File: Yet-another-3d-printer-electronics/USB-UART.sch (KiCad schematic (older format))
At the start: 13 parts

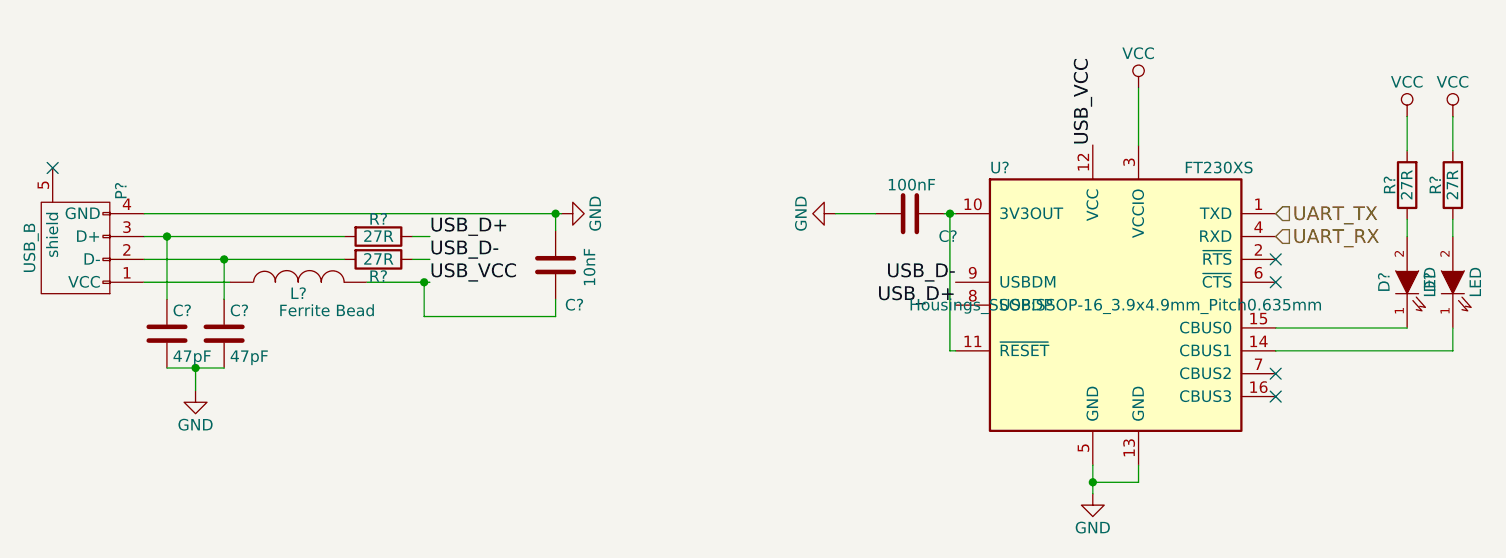
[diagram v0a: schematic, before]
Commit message: Add power section and remove fan heater
Add aoz1284pi buck conventer.

Signed-off-by: Mateusz Krawczuk <mat.krawczuk@gmail.com>
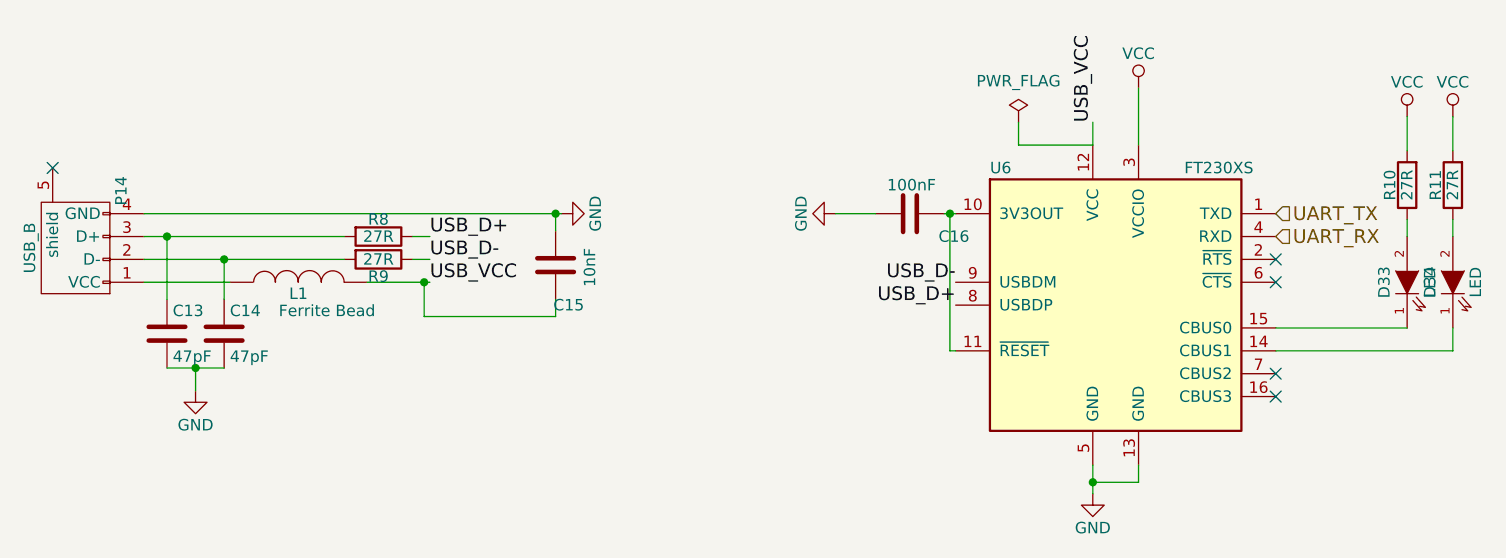
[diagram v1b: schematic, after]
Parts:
- gave numbers to parts that had none: 13
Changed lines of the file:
@@
 LIBS:valves
 LIBS:ftdi
+LIBS:aoz1284pi
 LIBS:Yet-another-3d-printer-electronics-cache
 EELAYER 25 0
@@
 $Descr A4 11693 8268
 encoding utf-8
-Sheet 3 4
+Sheet 3 5
 Title ""
 Date ""
@@
 NoConn ~ 7775 3175
 $Comp
-L FT230XS U?
+L FT230XS U6
 U 1 1 58B1D6DF
 P 7075 3375
-F 0 "U?" H 6525 3975 50  0000 L CNN
+F 0 "U6" H 6525 3975 50  0000 L CNN
 F 1 "FT230XS" H 7375 3975 50  0000 L CNN
-F 2 "Housings_SSOP:SSOP-16_3.9x4.9mm_Pitch0.635mm" H 7075 3375 50  0000 C CNN
+F 2 "Housings_SSOP:SSOP-16_3.9x4.9mm_Pitch0.635mm" H 7075 3375 50  0001 C CNN
 F 3 "" H 7075 3375 50  0000 C CNN
 	1    7075 3375
@@
 NoConn ~ 7775 3775
 $Comp
-L VCC #PWR?
+L VCC #PWR061
 U 1 1 58B1D6E9
 P 7175 2425
-F 0 "#PWR?" H 7175 2275 50  0001 C CNN
+F 0 "#PWR061" H 7175 2275 50  0001 C CNN
 F 1 "VCC" H 7175 2575 50  0000 C CNN
 F 2 "" H 7175 2425 50  0000 C CNN
@@
 $EndComp
 $Comp
-L GND #PWR?
+L GND #PWR062
 U 1 1 58B1D6EF
 P 6975 4200
-F 0 "#PWR?" H 6975 3950 50  0001 C CNN
+F 0 "#PWR062" H 6975 3950 50  0001 C CNN
 F 1 "GND" H 6975 4050 50  0000 C CNN
 F 2 "" H 6975 4200 50  0000 C CNN
@@
 $EndComp
 $Comp
-L USB_B-RESCUE-Yet-another-3d-printer-electronics P?
+L USB_B-RESCUE-Yet-another-3d-printer-electronics P14
 U 1 1 58B1D6F5
 P 2525 3075
-F 0 "P?" H 2725 2875 50  0000 C CNN
+F 0 "P14" H 2725 2875 50  0000 C CNN
 F 1 "USB_B" H 2475 3275 50  0000 C CNN
 F 2 "Connect:USB_B" V 2475 2975 50  0001 C CNN
@@
 $EndComp
 $Comp
-L R R?
+L R R8
 U 1 1 58B1D6FC
 P 3850 3075
-F 0 "R?" V 3775 3075 50  0000 C CNN
+F 0 "R8" V 3775 3075 50  0000 C CNN
 F 1 "27R" V 3850 3075 50  0000 C CNN
 F 2 "Resistors_SMD:R_0805_HandSoldering" V 3780 3075 50  0001 C CNN
@@
 $EndComp
 $Comp
-L R R?
+L R R9
 U 1 1 58B1D703
 P 3850 3175
-F 0 "R?" V 3925 3175 50  0000 C CNN
+F 0 "R9" V 3925 3175 50  0000 C CNN
 F 1 "27R" V 3850 3175 50  0000 C CNN
 F 2 "Resistors_SMD:R_0805_HandSoldering" V 3780 3175 50  0001 C CNN
@@
 USB_D-
 $Comp
-L C C?
+L C C16
 U 1 1 58B1D70C
 P 6175 2975
-F 0 "C?" V 6275 3100 50  0000 L CNN
+F 0 "C16" V 6275 3100 50  0000 L CNN
 F 1 "100nF" V 6050 2875 50  0000 L CNN
 F 2 "Capacitors_SMD:C_0805_HandSoldering" H 6213 2825 50  0001 C CNN
@@
 $EndComp
 $Comp
-L GND #PWR?
+L GND #PWR063
 U 1 1 58B1D713
 P 5850 2975
-F 0 "#PWR?" H 5850 2725 50  0001 C CNN
+F 0 "#PWR063" H 5850 2725 50  0001 C CNN
 F 1 "GND" H 5850 2825 50  0000 C CNN
 F 2 "" H 5850 2975 50  0000 C CNN
@@
 	0    1    1    0
 $EndComp
-Text Label 6975 2675 1    60   ~ 0
+Text Label 6975 2575 1    60   ~ 0
 USB_VCC
 $Comp
-L C C?
-U 1 1 58B1D71A
-P 2925 3500
-F 0 "C?" H 2950 3600 50  0000 L CNN
-F 1 "47pF" H 2950 3400 50  0000 L CNN
-F 2 "Capacitors_SMD:C_0805_HandSoldering" H 2963 3350 50  0001 C CNN
-F 3 "" H 2925 3500 50  0000 C CNN
-	1    2925 3500
-	1    0    0    -1
-$EndComp
-$Comp
-L C C?
+L C C14
 U 1 1 58B1D721
 P 3175 3500
-F 0 "C?" H 3200 3600 50  0000 L CNN
+F 0 "C14" H 3200 3600 50  0000 L CNN
 F 1 "47pF" H 3200 3400 50  0000 L CNN
 F 2 "Capacitors_SMD:C_0805_HandSoldering" H 3213 3350 50  0001 C CNN
@@
 NoConn ~ 2425 2775
 $Comp
-L GND #PWR?
+L GND #PWR064
 U 1 1 58B1D729
 P 3050 3750
-F 0 "#PWR?" H 3050 3500 50  0001 C CNN
+F 0 "#PWR064" H 3050 3500 50  0001 C CNN
 F 1 "GND" H 3050 3600 50  0000 C CNN
 F 2 "" H 3050 3750 50  0000 C CNN
@@
 USB_VCC
 $Comp
-L GND #PWR?
+L GND #PWR065
 U 1 1 58B1D732
 P 4650 2975
-F 0 "#PWR?" H 4650 2725 50  0001 C CNN
+F 0 "#PWR065" H 4650 2725 50  0001 C CNN
 F 1 "GND" H 4650 2825 50  0000 C CNN
 F 2 "" H 4650 2975 50  0000 C CNN
@@
 $EndComp
 $Comp
-L C C?
+L C C15
 U 1 1 58B1D738
 P 4625 3200
-F 0 "C?" H 4500 3375 50  0000 L CNN
+F 0 "C15" H 4500 3375 50  0000 L CNN
 F 1 "10nF" V 4475 3125 50  0000 L CNN
 F 2 "Capacitors_SMD:C_0805_HandSoldering" H 4663 3050 50  0001 C CNN
@@
 $EndComp
 $Comp
-L INDUCTOR L?
+L INDUCTOR L1
 U 1 1 58B1D73F
 P 3500 3275
-F 0 "L?" V 3450 3275 50  0000 C CNN
+F 0 "L1" V 3450 3275 50  0000 C CNN
 F 1 "Ferrite Bead" V 3375 3150 50  0000 C CNN
 F 2 "Choke_SMD:Choke_SMD_Wuerth-WE-PDF_Handsoldering" H 3500 3275 50  0001 C CNN
@@
 $EndComp
 $Comp
-L LED-RESCUE-Yet-another-3d-printer-electronics D?
+L LED-RESCUE-Yet-another-3d-printer-electronics D33
 U 1 1 58B1D746
 P 8350 3275
-F 0 "D?" H 8350 3375 50  0000 C CNN
+F 0 "D33" H 8350 3375 50  0000 C CNN
 F 1 "LED" H 8350 3175 50  0000 C CNN
 F 2 "LEDs:LED_0805" H 8350 3275 50  0001 C CNN
@@
 $EndComp
 $Comp
-L LED-RESCUE-Yet-another-3d-printer-electronics D?
+L LED-RESCUE-Yet-another-3d-printer-electronics D34
 U 1 1 58B1D74D
 P 8550 3275
-F 0 "D?" H 8550 3375 50  0000 C CNN
+F 0 "D34" H 8550 3375 50  0000 C CNN
 F 1 "LED" H 8550 3175 50  0000 C CNN
 F 2 "LEDs:LED_0805" H 8550 3275 50  0001 C CNN
@@
 $EndComp
 $Comp
-L R R?
+L R R10
 U 1 1 58B1D754
 P 8350 2850
-F 0 "R?" V 8425 2850 50  0000 C CNN
+F 0 "R10" V 8425 2850 50  0000 C CNN
 F 1 "27R" V 8350 2850 50  0000 C CNN
 F 2 "Resistors_SMD:R_0805_HandSoldering" V 8280 2850 50  0001 C CNN
@@
 $EndComp
 $Comp
-L R R?
+L R R11
 U 1 1 58B1D75B
 P 8550 2850
-F 0 "R?" V 8625 2850 50  0000 C CNN
+F 0 "R11" V 8625 2850 50  0000 C CNN
 F 1 "27R" V 8550 2850 50  0000 C CNN
 F 2 "Resistors_SMD:R_0805_HandSoldering" V 8480 2850 50  0001 C CNN
@@
 $EndComp
 $Comp
-L VCC #PWR?
+L VCC #PWR066
 U 1 1 58B1D762
 P 8350 2550
-F 0 "#PWR?" H 8350 2400 50  0001 C CNN
+F 0 "#PWR066" H 8350 2400 50  0001 C CNN
 F 1 "VCC" H 8350 2700 50  0000 C CNN
 F 2 "" H 8350 2550 50  0000 C CNN
@@
 $EndComp
 $Comp
-L VCC #PWR?
+L VCC #PWR067
 U 1 1 58B1D768
 P 8550 2550
-F 0 "#PWR?" H 8550 2400 50  0001 C CNN
+F 0 "#PWR067" H 8550 2400 50  0001 C CNN
 F 1 "VCC" H 8550 2700 50  0000 C CNN
 F 2 "" H 8550 2550 50  0000 C CNN
@@
 	1    0    0    -1
 $EndComp
-Wire Wire Line
-	7175 2425 7175 2675
-Wire Wire Line
-	6975 4075 6975 4200
-Wire Wire Line
-	6375 2975 6325 2975
-Wire Wire Line
-	6025 2975 5850 2975
-Wire Wire Line
-	6350 2975 6350 3575
-Wire Wire Line
-	6350 3575 6375 3575
-Connection ~ 6350 2975
-Wire Wire Line
-	7175 4075 7175 4150
-Wire Wire Line
-	7175 4150 6975 4150
-Connection ~ 6975 4150
-Wire Wire Line
-	2825 2975 4650 2975
-Wire Wire Line
-	2825 3175 3700 3175
-Wire Wire Line
-	2825 3075 3700 3075
-Wire Wire Line
-	2925 3075 2925 3350
-Connection ~ 2925 3075
-Wire Wire Line
-	3175 3175 3175 3350
-Connection ~ 3175 3175
-Wire Wire Line
-	2925 3650 3175 3650
-Wire Wire Line
-	3050 3650 3050 3750
-Connection ~ 3050 3650
-Wire Wire Line
-	4000 3075 4075 3075
-Wire Wire Line
-	4000 3175 4075 3175
-Wire Wire Line
-	4050 3275 4050 3425
-Wire Wire Line
-	4050 3425 4625 3425
-Wire Wire Line
-	4625 3425 4625 3350
-Connection ~ 4050 3275
-Wire Wire Line
-	4625 3050 4625 2975
-Connection ~ 4625 2975
-Wire Wire Line
-	3800 3275 4075 3275
-Wire Wire Line
-	3200 3275 2825 3275
-Wire Wire Line
-	8350 3475 7775 3475
-Wire Wire Line
-	7775 3575 8550 3575
-Wire Wire Line
-	8550 3575 8550 3475
-Wire Wire Line
-	8350 3000 8350 3075
-Wire Wire Line
-	8550 3075 8550 3000
-Wire Wire Line
-	8350 2700 8350 2550
-Wire Wire Line
-	8550 2700 8550 2550
 Text HLabel 7775 2975 2    60   Input ~ 0
 UART_TX
 Text HLabel 7775 3075 2    60   Input ~ 0
 UART_RX
+$Comp
+L C C13
+U 1 1 58B1D71A
+P 2925 3500
+F 0 "C13" H 2950 3600 50  0000 L CNN
+F 1 "47pF" H 2950 3400 50  0000 L CNN
+F 2 "Capacitors_SMD:C_0805_HandSoldering" H 2963 3350 50  0001 C CNN
+F 3 "" H 2925 3500 50  0000 C CNN
+	1    2925 3500
+	1    0    0    -1
+$EndComp
+Wire Wire Line
+	7175 2425 7175 2675
+Wire Wire Line
+	6975 4075 6975 4200
+Wire Wire Line
+	6375 2975 6325 2975
+Wire Wire Line
+	6025 2975 5850 2975
+Wire Wire Line
+	6350 2975 6350 3575
+Wire Wire Line
+	6350 3575 6375 3575
+Connection ~ 6350 2975
+Wire Wire Line
+	7175 4075 7175 4150
+Wire Wire Line
+	7175 4150 6975 4150
+Connection ~ 6975 4150
+Wire Wire Line
+	2825 2975 4650 2975
+Wire Wire Line
+	2825 3175 3700 3175
+Wire Wire Line
+	2825 3075 3700 3075
+Wire Wire Line
+	2925 3075 2925 3350
+Connection ~ 2925 3075
+Wire Wire Line
+	3175 3175 3175 3350
+Connection ~ 3175 3175
+Wire Wire Line
+	2925 3650 3175 3650
+Wire Wire Line
+	3050 3650 3050 3750
+Connection ~ 3050 3650
+Wire Wire Line
+	4000 3075 4075 3075
+Wire Wire Line
+	4000 3175 4075 3175
+Wire Wire Line
+	4050 3275 4050 3425
+Wire Wire Line
+	4050 3425 4625 3425
+Wire Wire Line
+	4625 3425 4625 3350
+Connection ~ 4050 3275
+Wire Wire Line
+	4625 3050 4625 2975
+Connection ~ 4625 2975
+Wire Wire Line
+	3800 3275 4075 3275
+Wire Wire Line
+	3200 3275 2825 3275
+Wire Wire Line
+	8350 3475 7775 3475
+Wire Wire Line
+	7775 3575 8550 3575
+Wire Wire Line
+	8550 3575 8550 3475
+Wire Wire Line
+	8350 3000 8350 3075
+Wire Wire Line
+	8550 3075 8550 3000
+Wire Wire Line
+	8350 2700 8350 2550
+Wire Wire Line
+	8550 2700 8550 2550
+Wire Wire Line
+	6975 2675 6975 2575
+$Comp
+L PWR_FLAG #FLG068
+U 1 1 58B14734
+P 6650 2575
+F 0 "#FLG068" H 6650 2670 50  0001 C CNN
+F 1 "PWR_FLAG" H 6650 2755 50  0000 C CNN
+F 2 "" H 6650 2575 50  0000 C CNN
+F 3 "" H 6650 2575 50  0000 C CNN
+	1    6650 2575
+	1    0    0    -1
+$EndComp
+Wire Wire Line
+	6650 2575 6650 2675
+Wire Wire Line
+	6650 2675 6975 2675
 $EndSCHEMATC

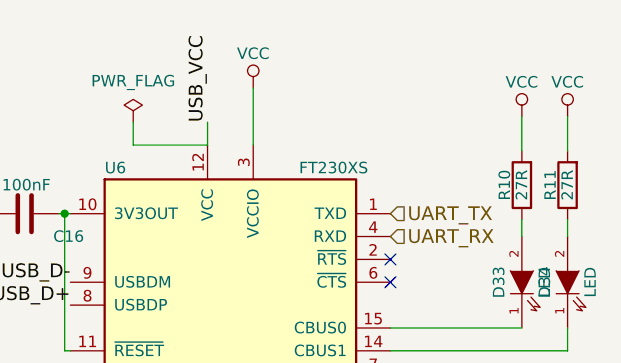
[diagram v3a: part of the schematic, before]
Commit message: Add additional stepstick, hotend fan and heater and temperature sensor
Extruder stepsticks have independ enables pins. Vcc was replace by valid
power source.

Signed-off-by: Mateusz Krawczuk <mat.krawczuk@gmail.com>
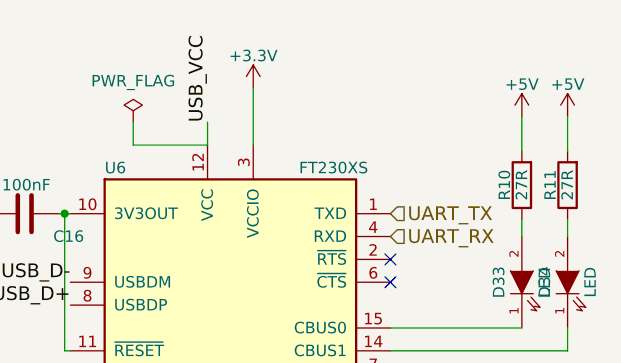
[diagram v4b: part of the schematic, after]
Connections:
- net VCC renamed +5V
- net +5V: no longer U6.3 (VCCIO)
- new net +3V3: U6.3 (VCCIO)
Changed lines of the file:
@@
 NoConn ~ 7775 3775
 $Comp
-L VCC #PWR061
-U 1 1 58B1D6E9
-P 7175 2425
-F 0 "#PWR061" H 7175 2275 50  0001 C CNN
-F 1 "VCC" H 7175 2575 50  0000 C CNN
-F 2 "" H 7175 2425 50  0000 C CNN
-F 3 "" H 7175 2425 50  0000 C CNN
-	1    7175 2425
-	1    0    0    -1
-$EndComp
-$Comp
-L GND #PWR062
+L GND #PWR074
 U 1 1 58B1D6EF
 P 6975 4200
-F 0 "#PWR062" H 6975 3950 50  0001 C CNN
+F 0 "#PWR074" H 6975 3950 50  0001 C CNN
 F 1 "GND" H 6975 4050 50  0000 C CNN
 F 2 "" H 6975 4200 50  0000 C CNN
@@
 $EndComp
 $Comp
-L GND #PWR063
+L GND #PWR075
 U 1 1 58B1D713
 P 5850 2975
-F 0 "#PWR063" H 5850 2725 50  0001 C CNN
+F 0 "#PWR075" H 5850 2725 50  0001 C CNN
 F 1 "GND" H 5850 2825 50  0000 C CNN
 F 2 "" H 5850 2975 50  0000 C CNN
@@
 NoConn ~ 2425 2775
 $Comp
-L GND #PWR064
+L GND #PWR076
 U 1 1 58B1D729
 P 3050 3750
-F 0 "#PWR064" H 3050 3500 50  0001 C CNN
+F 0 "#PWR076" H 3050 3500 50  0001 C CNN
 F 1 "GND" H 3050 3600 50  0000 C CNN
 F 2 "" H 3050 3750 50  0000 C CNN
@@
 USB_VCC
 $Comp
-L GND #PWR065
+L GND #PWR077
 U 1 1 58B1D732
 P 4650 2975
-F 0 "#PWR065" H 4650 2725 50  0001 C CNN
+F 0 "#PWR077" H 4650 2725 50  0001 C CNN
 F 1 "GND" H 4650 2825 50  0000 C CNN
 F 2 "" H 4650 2975 50  0000 C CNN
@@
 	-1   0    0    1
 $EndComp
-$Comp
-L VCC #PWR066
-U 1 1 58B1D762
-P 8350 2550
-F 0 "#PWR066" H 8350 2400 50  0001 C CNN
-F 1 "VCC" H 8350 2700 50  0000 C CNN
-F 2 "" H 8350 2550 50  0000 C CNN
-F 3 "" H 8350 2550 50  0000 C CNN
-	1    8350 2550
-	1    0    0    -1
-$EndComp
-$Comp
-L VCC #PWR067
-U 1 1 58B1D768
-P 8550 2550
-F 0 "#PWR067" H 8550 2400 50  0001 C CNN
-F 1 "VCC" H 8550 2700 50  0000 C CNN
-F 2 "" H 8550 2550 50  0000 C CNN
-F 3 "" H 8550 2550 50  0000 C CNN
-	1    8550 2550
-	1    0    0    -1
-$EndComp
 Text HLabel 7775 2975 2    60   Input ~ 0
 UART_TX
@@
 	6975 2675 6975 2575
 $Comp
-L PWR_FLAG #FLG068
+L PWR_FLAG #FLG078
 U 1 1 58B14734
 P 6650 2575
-F 0 "#FLG068" H 6650 2670 50  0001 C CNN
+F 0 "#FLG078" H 6650 2670 50  0001 C CNN
 F 1 "PWR_FLAG" H 6650 2755 50  0000 C CNN
 F 2 "" H 6650 2575 50  0000 C CNN
@@
 Wire Wire Line
 	6650 2675 6975 2675
+$Comp
+L +3.3V #PWR079
+U 1 1 5900AC18
+P 7175 2425
+F 0 "#PWR079" H 7175 2275 50  0001 C CNN
+F 1 "+3.3V" H 7175 2565 50  0000 C CNN
+F 2 "" H 7175 2425 50  0001 C CNN
+F 3 "" H 7175 2425 50  0001 C CNN
+	1    7175 2425
+	1    0    0    -1
+$EndComp
+$Comp
+L +5V #PWR080
+U 1 1 5900E466
+P 8350 2550
+F 0 "#PWR080" H 8350 2400 50  0001 C CNN
+F 1 "+5V" H 8350 2690 50  0000 C CNN
+F 2 "" H 8350 2550 50  0001 C CNN
+F 3 "" H 8350 2550 50  0001 C CNN
+	1    8350 2550
+	1    0    0    -1
+$EndComp
+$Comp
+L +5V #PWR081
+U 1 1 5900E49F
+P 8550 2550
+F 0 "#PWR081" H 8550 2400 50  0001 C CNN
+F 1 "+5V" H 8550 2690 50  0000 C CNN
+F 2 "" H 8550 2550 50  0001 C CNN
+F 3 "" H 8550 2550 50  0001 C CNN
+	1    8550 2550
+	1    0    0    -1
+$EndComp
 $EndSCHEMATC

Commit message: Choose footprints for some components
Signed-off-by: Mateusz Krawczuk <mat.krawczuk@gmail.com>
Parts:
- R10, R11, R8, R9: footprint Resistors_SMD:R_0805_HandSoldering -> Resistors_SMD:R_0603_HandSoldering
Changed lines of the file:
@@
 NoConn ~ 7775 3775
 $Comp
-L GND #PWR78
+L GND #PWR075
 U 1 1 58B1D6EF
 P 6975 4200
-F 0 "#PWR78" H 6975 3950 50  0001 C CNN
+F 0 "#PWR075" H 6975 3950 50  0001 C CNN
 F 1 "GND" H 6975 4050 50  0000 C CNN
 F 2 "" H 6975 4200 50  0000 C CNN
@@
 F 0 "R8" V 3775 3075 50  0000 C CNN
 F 1 "27R" V 3850 3075 50  0000 C CNN
-F 2 "Resistors_SMD:R_0805_HandSoldering" V 3780 3075 50  0001 C CNN
+F 2 "Resistors_SMD:R_0603_HandSoldering" V 3780 3075 50  0001 C CNN
 F 3 "" H 3850 3075 50  0000 C CNN
 	1    3850 3075
@@
 F 0 "R9" V 3925 3175 50  0000 C CNN
 F 1 "27R" V 3850 3175 50  0000 C CNN
-F 2 "Resistors_SMD:R_0805_HandSoldering" V 3780 3175 50  0001 C CNN
+F 2 "Resistors_SMD:R_0603_HandSoldering" V 3780 3175 50  0001 C CNN
 F 3 "" H 3850 3175 50  0000 C CNN
 	1    3850 3175
@@
 $EndComp
 $Comp
-L GND #PWR77
+L GND #PWR076
 U 1 1 58B1D713
 P 5850 2975
-F 0 "#PWR77" H 5850 2725 50  0001 C CNN
+F 0 "#PWR076" H 5850 2725 50  0001 C CNN
 F 1 "GND" H 5850 2825 50  0000 C CNN
 F 2 "" H 5850 2975 50  0000 C CNN
@@
 NoConn ~ 2425 2775
 $Comp
-L GND #PWR75
+L GND #PWR077
 U 1 1 58B1D729
 P 3050 3750
-F 0 "#PWR75" H 3050 3500 50  0001 C CNN
+F 0 "#PWR077" H 3050 3500 50  0001 C CNN
 F 1 "GND" H 3050 3600 50  0000 C CNN
 F 2 "" H 3050 3750 50  0000 C CNN
@@
 USB_VCC
 $Comp
-L GND #PWR76
+L GND #PWR078
 U 1 1 58B1D732
 P 4650 2975
-F 0 "#PWR76" H 4650 2725 50  0001 C CNN
+F 0 "#PWR078" H 4650 2725 50  0001 C CNN
 F 1 "GND" H 4650 2825 50  0000 C CNN
 F 2 "" H 4650 2975 50  0000 C CNN
@@
 F 0 "R10" V 8425 2850 50  0000 C CNN
 F 1 "27R" V 8350 2850 50  0000 C CNN
-F 2 "Resistors_SMD:R_0805_HandSoldering" V 8280 2850 50  0001 C CNN
+F 2 "Resistors_SMD:R_0603_HandSoldering" V 8280 2850 50  0001 C CNN
 F 3 "" H 8350 2850 50  0000 C CNN
 	1    8350 2850
@@
 F 0 "R11" V 8625 2850 50  0000 C CNN
 F 1 "27R" V 8550 2850 50  0000 C CNN
-F 2 "Resistors_SMD:R_0805_HandSoldering" V 8480 2850 50  0001 C CNN
+F 2 "Resistors_SMD:R_0603_HandSoldering" V 8480 2850 50  0001 C CNN
 F 3 "" H 8550 2850 50  0000 C CNN
 	1    8550 2850
@@
 	6975 2675 6975 2575
 $Comp
-L PWR_FLAG #FLG1
+L PWR_FLAG #FLG079
 U 1 1 58B14734
 P 6650 2575
-F 0 "#FLG1" H 6650 2670 50  0001 C CNN
+F 0 "#FLG079" H 6650 2670 50  0001 C CNN
 F 1 "PWR_FLAG" H 6650 2755 50  0000 C CNN
 F 2 "" H 6650 2575 50  0000 C CNN
@@
 	6650 2675 6975 2675
 $Comp
-L +3.3V #PWR79
+L +3.3V #PWR080
 U 1 1 5900AC18
 P 7175 2425
-F 0 "#PWR79" H 7175 2275 50  0001 C CNN
+F 0 "#PWR080" H 7175 2275 50  0001 C CNN
 F 1 "+3.3V" H 7175 2565 50  0000 C CNN
 F 2 "" H 7175 2425 50  0001 C CNN
@@
 $EndComp
 $Comp
-L +5V #PWR80
+L +5V #PWR081
 U 1 1 5900E466
 P 8350 2550
-F 0 "#PWR80" H 8350 2400 50  0001 C CNN
+F 0 "#PWR081" H 8350 2400 50  0001 C CNN
 F 1 "+5V" H 8350 2690 50  0000 C CNN
 F 2 "" H 8350 2550 50  0001 C CNN
@@
 $EndComp
 $Comp
-L +5V #PWR81
+L +5V #PWR082
 U 1 1 5900E49F
 P 8550 2550
-F 0 "#PWR81" H 8550 2400 50  0001 C CNN
+F 0 "#PWR082" H 8550 2400 50  0001 C CNN
 F 1 "+5V" H 8550 2690 50  0000 C CNN
 F 2 "" H 8550 2550 50  0001 C CNN
